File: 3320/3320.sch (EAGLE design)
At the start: 70 parts, among them IC1 OPA2134P, IC2 OPA2134P, X1 2516-

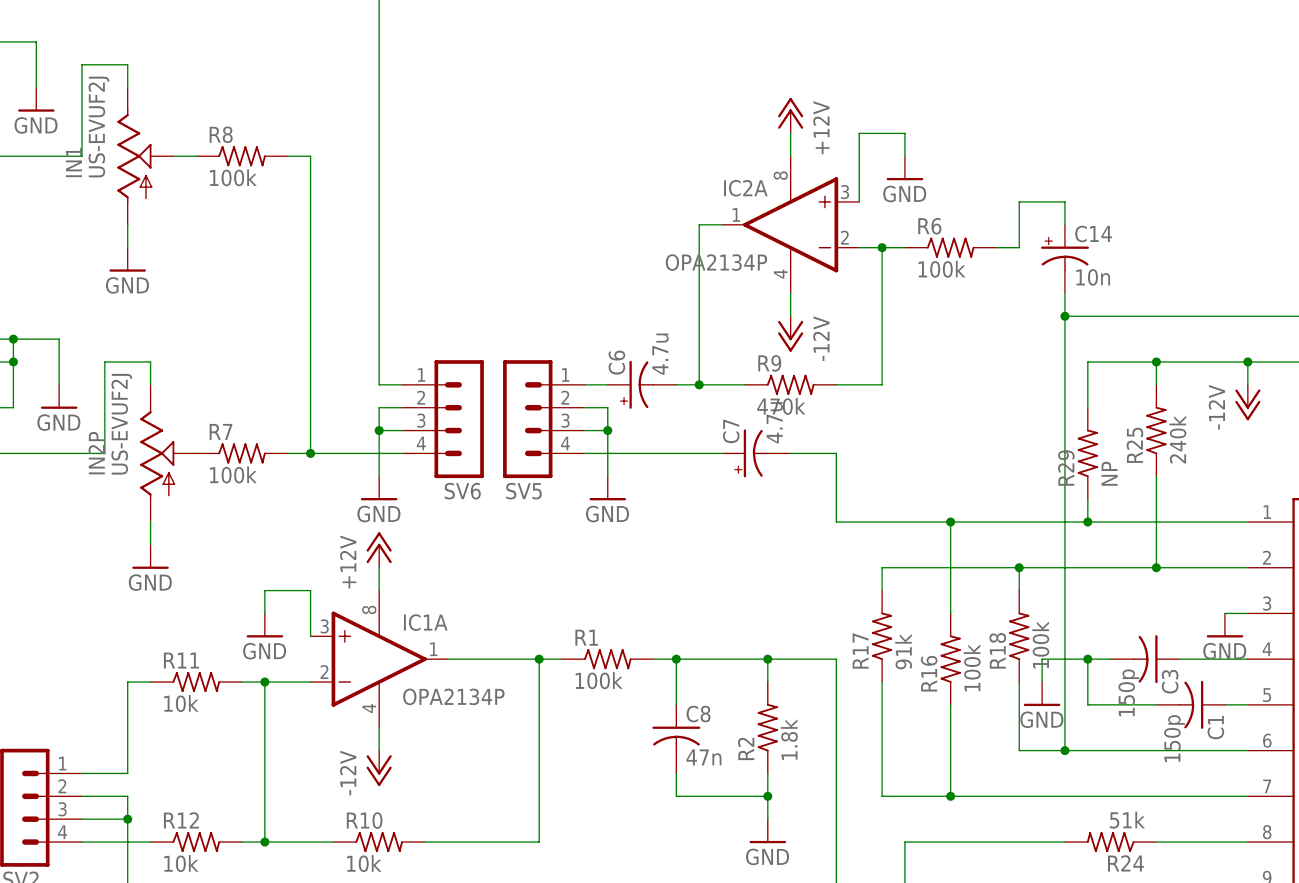
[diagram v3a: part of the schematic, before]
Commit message: made post fab component changes to 3320 and some fixes to svf board
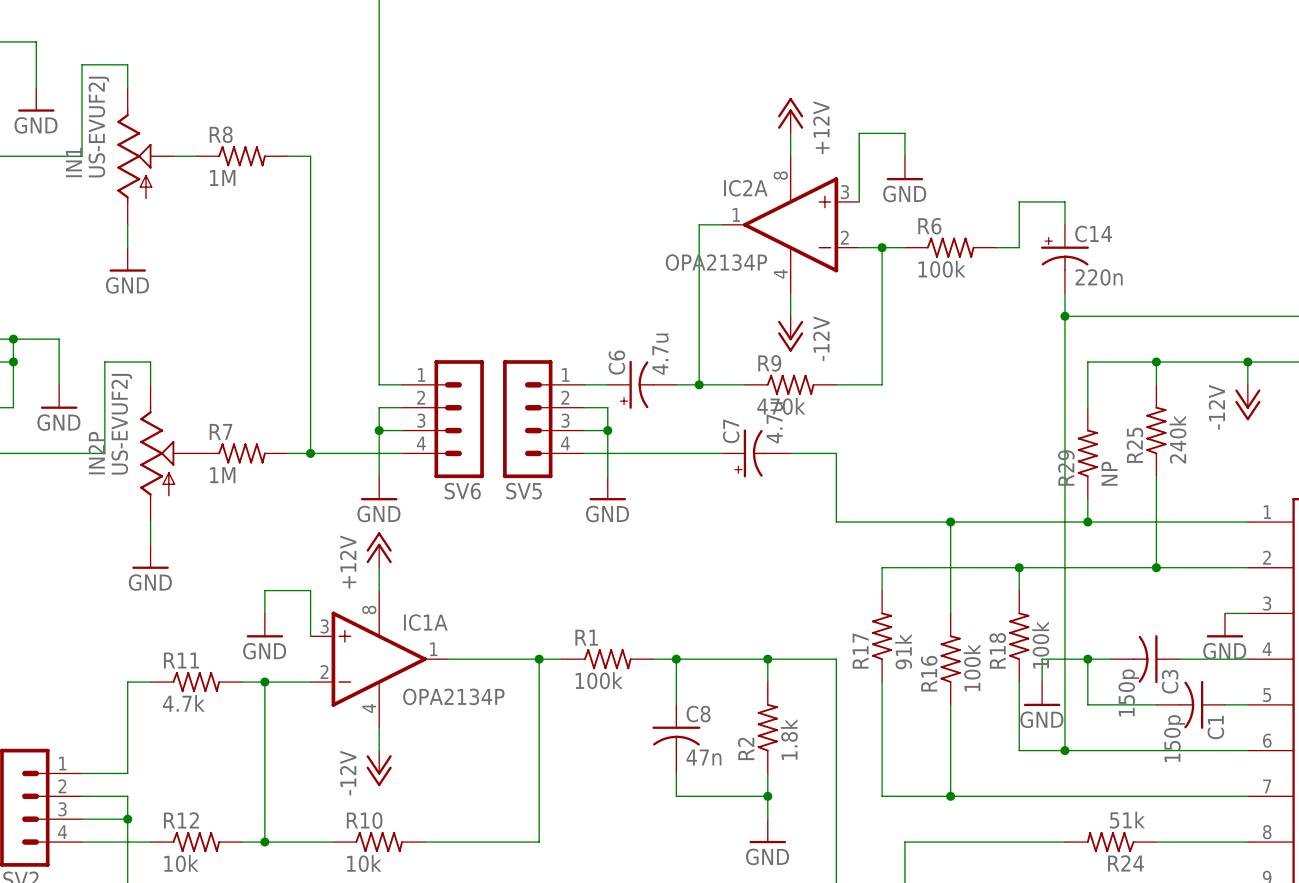
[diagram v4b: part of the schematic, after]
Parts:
- C14: value 10n -> 220n
- R11: value 10k -> 4.7k
- R7, R8: value 100k -> 1M
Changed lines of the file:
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@@
 <part name="P-2" library="dan" deviceset="-12V" device=""/>
 <part name="R10" library="dan" deviceset="R-US_" device="0207/2V" value="10k"/>
-<part name="R11" library="dan" deviceset="R-US_" device="0207/2V" value="10k"/>
+<part name="R11" library="dan" deviceset="R-US_" device="0207/2V" value="4.7k"/>
 <part name="R12" library="dan" deviceset="R-US_" device="0207/2V" value="10k"/>
 <part name="C8" library="dan" deviceset="C-US" device="050-025X075" value="47n"/>
@@
 <part name="IN2" library="dan" deviceset="PJ301BM" device=""/>
 <part name="GND4" library="dan" deviceset="GND" device=""/>
-<part name="R7" library="dan" deviceset="R-US_" device="0204/7" value="100k"/>
-<part name="R8" library="dan" deviceset="R-US_" device="0204/7" value="100k"/>
+<part name="R7" library="dan" deviceset="R-US_" device="0204/7" value="1M"/>
+<part name="R8" library="dan" deviceset="R-US_" device="0204/7" value="1M"/>
 <part name="GND20" library="dan" deviceset="GND" device=""/>
 <part name="GND21" library="dan" deviceset="GND" device=""/>
@@
 <part name="R26" library="dan" deviceset="R-US_" device="0207/2V" value="240k"/>
 <part name="R27" library="dan" deviceset="R-US_" device="0207/2V" value="240k"/>
-<part name="C14" library="dan" deviceset="CPOL-US" device="E2.5-6" value="10n"/>
+<part name="C14" library="dan" deviceset="CPOL-US" device="E2.5-6" value="220n"/>
 <part name="C15" library="dan" deviceset="CPOL-US" device="E2.5-6" value="2.2u"/>
 <part name="C16" library="dan" deviceset="CPOL-US" device="E2.5-6" value="2.2u"/>

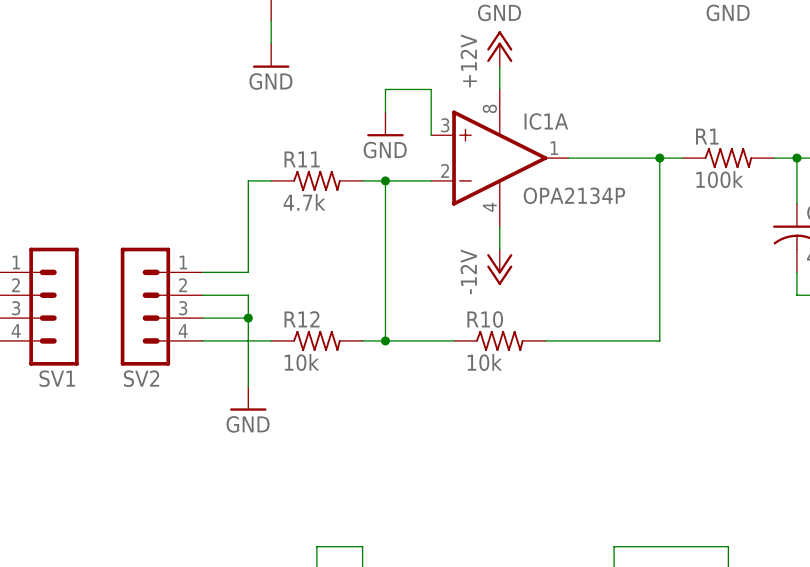
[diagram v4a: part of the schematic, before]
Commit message: respun the svf.  changed a few components on the 3320
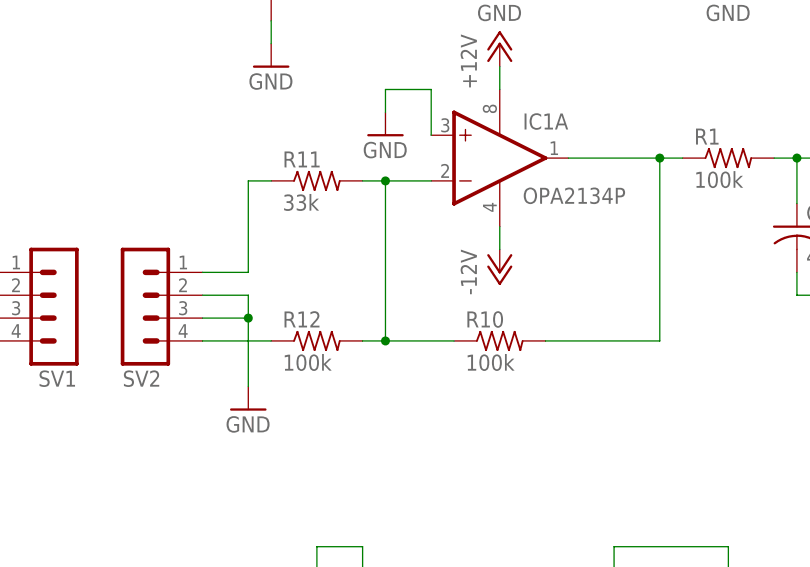
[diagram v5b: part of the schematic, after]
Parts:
- R10, R12: value 10k -> 100k
- R11: value 4.7k -> 33k
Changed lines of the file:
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@@
 <part name="P+2" library="dan" deviceset="+12V" device=""/>
 <part name="P-2" library="dan" deviceset="-12V" device=""/>
-<part name="R10" library="dan" deviceset="R-US_" device="0207/2V" value="10k"/>
-<part name="R11" library="dan" deviceset="R-US_" device="0207/2V" value="4.7k"/>
-<part name="R12" library="dan" deviceset="R-US_" device="0207/2V" value="10k"/>
+<part name="R10" library="dan" deviceset="R-US_" device="0207/2V" value="100k"/>
+<part name="R11" library="dan" deviceset="R-US_" device="0207/2V" value="33k"/>
+<part name="R12" library="dan" deviceset="R-US_" device="0207/2V" value="100k"/>
 <part name="C8" library="dan" deviceset="C-US" device="050-025X075" value="47n"/>
 <part name="GND5" library="dan" deviceset="GND" device=""/>
